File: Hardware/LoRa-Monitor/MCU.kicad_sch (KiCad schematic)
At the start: 20 parts, among them U1 ESP32-S3-WROOM-1

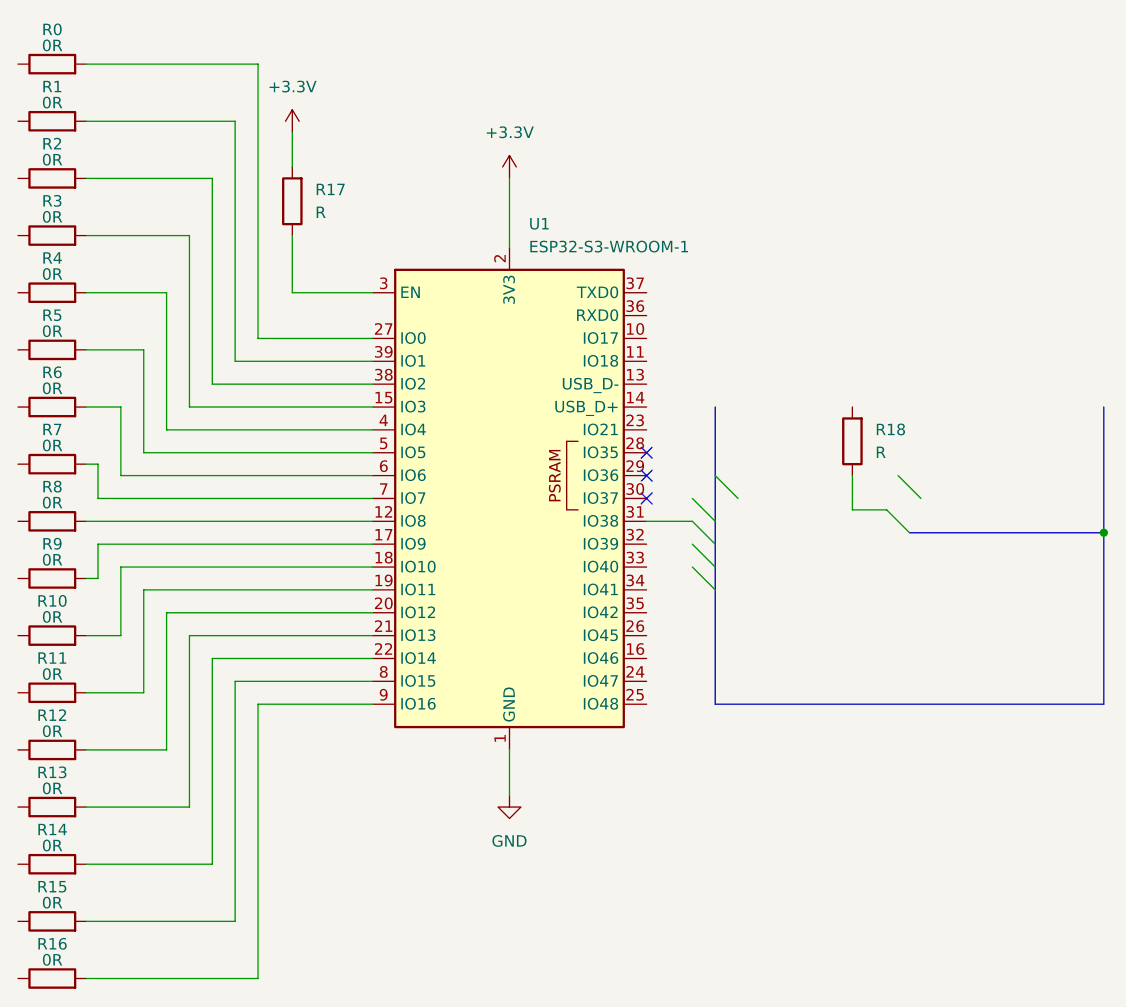
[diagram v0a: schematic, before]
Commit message: Added PSU
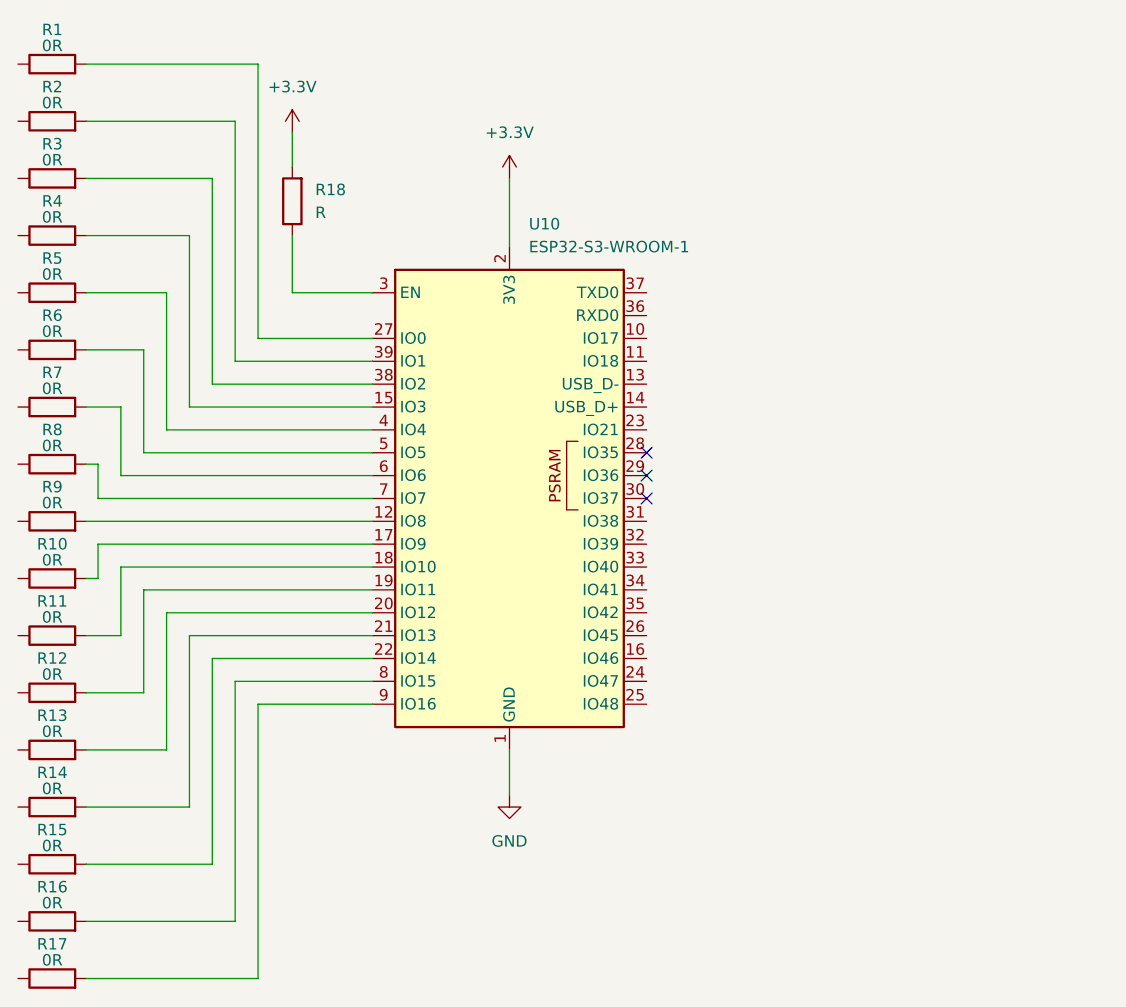
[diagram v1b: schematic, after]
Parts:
- removed R18: R, Resistor_SMD:R_0805_2012Metric, symbol Device:R
- removed U1: ESP32-S3-WROOM-1, Package_DFN_QFN:QFN-56-1EP_7x7mm_P0.4mm_EP4x4mm, symbol RF_Module:ESP32-S3-WROOM-1
- added U10: ESP32-S3-WROOM-1, RF_Module:ESP32-S3-WROOM-1, symbol RF_Module:ESP32-S3-WROOM-1
- renumbered R0 to R1, R9 to R10, R10 to R11, R11 to R12, R12 to R13, R13 to R14, R14 to R15, R15 to R16, R16 to R17, R17 to R18, R1 to R2, R2 to R3, R3 to R4, R4 to R5, R5 to R6, R6 to R7, R7 to R8, R8 to R9
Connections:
- net +3.3V: now also U10.2 (3V3)
- net GND: now also U10.1 (GND), U10.40 (GND), U10.41 (GND)
- net at R16.2: now also U10.8 (IO15)
- net at R2.2: now also U10.39 (IO1)
- net at R9.2: now also U10.12 (IO8)
- net at R6.2: now also U10.5 (IO5)
- net at R1.2: now also U10.27 (IO0)
- net at R15.2: now also U10.22 (IO14)
- net at R5.2: now also U10.4 (IO4)
- net at R4.2: now also U10.15 (IO3)
- net at R10.2: now also U10.17 (IO9)
- net at R11.2: now also U10.18 (IO10)
- net at R12.2: now also U10.19 (IO11)
- net at R13.2: now also U10.20 (IO12)
- net at R14.2: now also U10.21 (IO13)
- net at R18.1: now also U10.3 (EN)
- net at R3.2: now also U10.38 (IO2)
- net at R7.2: now also U10.6 (IO6)
- net at R8.2: now also U10.7 (IO7)
- net at R17.2: now also U10.9 (IO16)

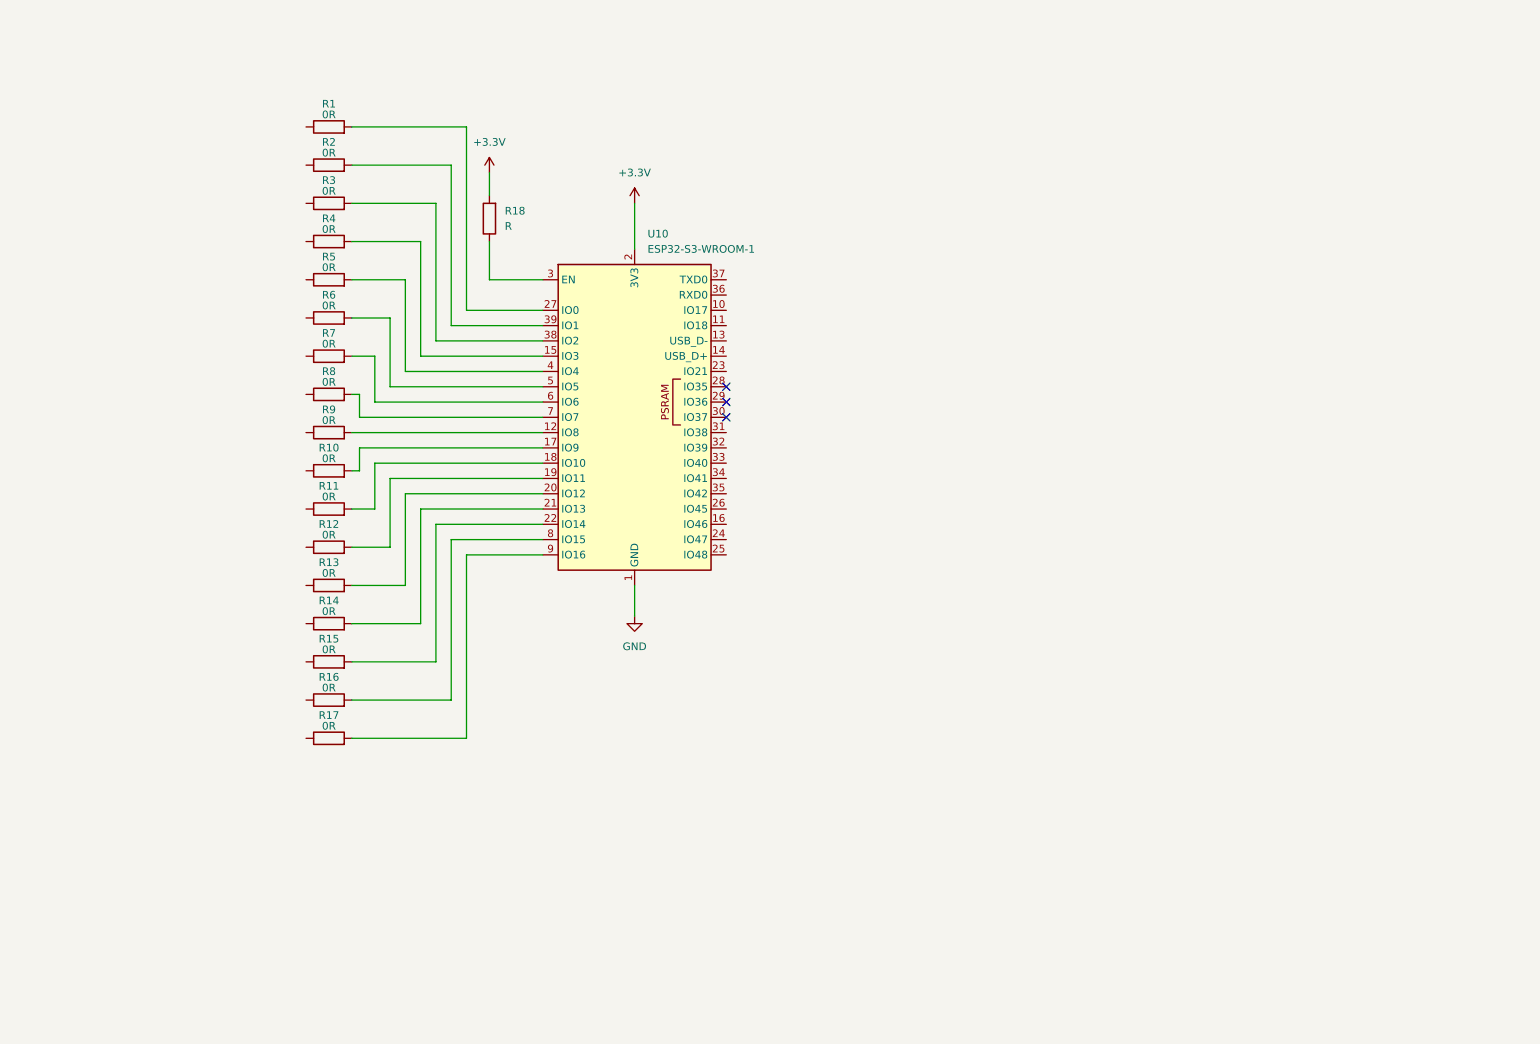
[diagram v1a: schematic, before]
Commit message: Finished Energy Meter Module, started LoRa Module and MCU.
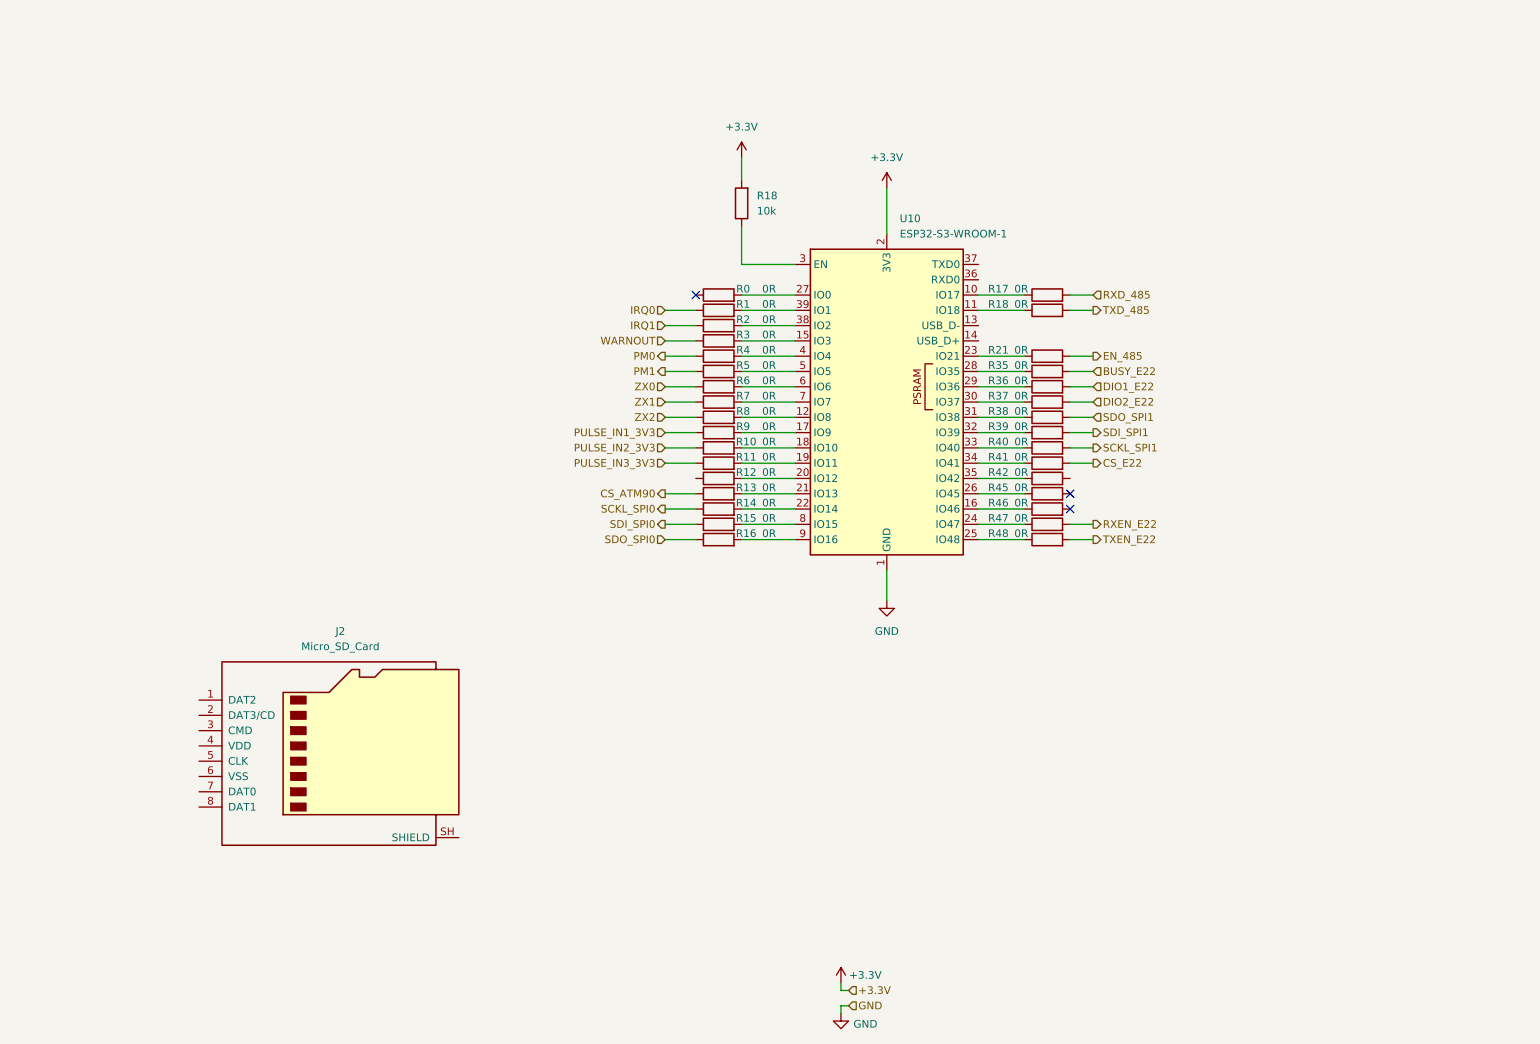
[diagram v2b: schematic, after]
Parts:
- added J2: Micro_SD_Card, Connector_Card:microSD_HC_Molex_47219-2001, symbol Connector:Micro_SD_Card
- added R0, R18, R21, R35, R36, R37, R38, R39, R40, R41, R42, R45, R46, R47, R48: 0R, Resistor_SMD:R_0805_2012Metric, symbol Device:R
- R18: value R -> 10k
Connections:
- net SDO_SPI0: now reaches R16.1
- net at U10.8 (IO15): now also R15.2; no longer R16.2
- net IRQ1: now reaches R2.1
- net at R2.2: now also U10.38 (IO2); no longer U10.39 (IO1)
- net PULSE_IN1_3V3: now reaches R9.1
- net at U10.12 (IO8): now also R8.2; no longer R9.2
- net at U10.10 (IO17): now also R17.1
- net at U10.11 (IO18): now also R18.1
- net at R4.2: now also U10.4 (IO4); no longer U10.15 (IO3)
- net at U10.16 (IO46): now also R46.1
- net at U10.17 (IO9): now also R9.2; no longer R10.2
- net at U10.18 (IO10): now also R10.2; no longer R11.2
- net at U10.19 (IO11): now also R11.2; no longer R12.2
- net at R13.2: now also U10.21 (IO13); no longer U10.20 (IO12)
- net at R14.2: now also U10.22 (IO14); no longer U10.21 (IO13)
- net at U10.23 (IO21): now also R21.1
- net at U10.24 (IO47): now also R47.1
- net at U10.25 (IO48): now also R48.1
- net at U10.26 (IO45): now also R45.1
- net at U10.27 (IO0): now also R0.2; no longer R1.2
- net at U10.28 (IO35): now also R35.1
- net at U10.29 (IO36): now also R36.1
- net at U10.30 (IO37): now also R37.1
- net at U10.31 (IO38): now also R38.1
- net at U10.32 (IO39): now also R39.1
- net at U10.33 (IO40): now also R40.1
- net at U10.34 (IO41): now also R41.1
- net at U10.35 (IO42): now also R42.1
- net at R3.2: now also U10.15 (IO3); no longer U10.38 (IO2)
- net at R5.2: now also U10.5 (IO5); no longer U10.4 (IO4)
- net at R6.2: now also U10.6 (IO6); no longer U10.5 (IO5)
- net at R7.2: now also U10.7 (IO7); no longer U10.6 (IO6)
- net at U10.9 (IO16): now also R16.2; no longer R17.2
- net ZX0: now reaches R6.1
- net IRQ0: now reaches R1.1
- net SDI_SPI0: now reaches R15.1
- net PM1: now reaches R5.1
- net PULSE_IN3_3V3: now reaches R11.1
- net PULSE_IN2_3V3: now reaches R10.1
- net CS_ATM90: now reaches R13.1
- net ZX1: now reaches R7.1
- net SCKL_SPI0: now reaches R14.1
- net WARNOUT: now reaches R3.1
- net PM0: now reaches R4.1
- net ZX2: now reaches R8.1
- new net: R12.2, U10.20 (IO12)
- new net: R1.2, U10.39 (IO1)
- new net BUSY_E22: R35.2
- new net CS_E22: R41.2
- new net DIO1_E22: R36.2
- new net DIO2_E22: R37.2
- new net EN_485: R21.2
- new net RXD_485: R17.2
- new net RXEN_E22: R47.2
- new net SCKL_SPI1: R40.2
- new net SDI_SPI1: R39.2
- new net SDO_SPI1: R38.2
- new net TXD_485: R18.2
- new net TXEN_E22: R48.2
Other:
- moved on the sheet: R18, U10

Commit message: Finished MCU and Lora modules. Finished Connectors sheet
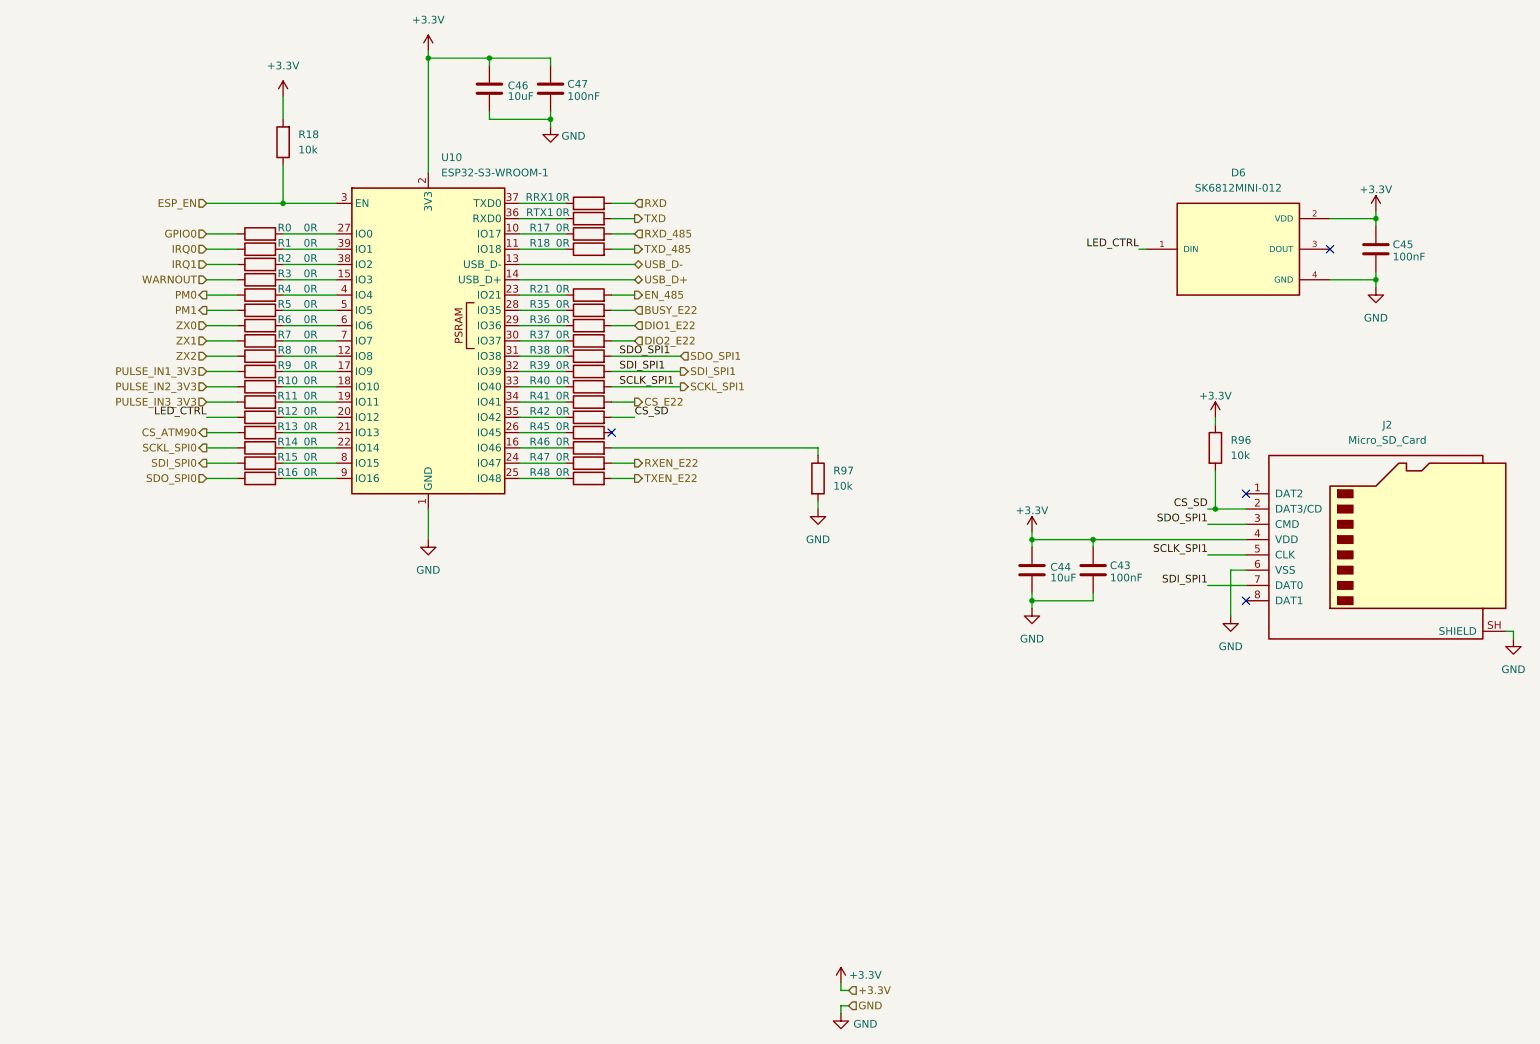
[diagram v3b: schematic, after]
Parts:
- added C43, C45, C47: 100nF, Capacitor_SMD:C_0805_2012Metric, symbol Device:C
- added C44, C46: 10uF, Capacitor_SMD:C_0805_2012Metric, symbol Device:C
- added D6: SK6812MINI-012, DeviceComponents:LED_SK6812MINI-012, symbol DeviceComponents:SK6812MINI-012
- added R96, R97: 10k, Resistor_SMD:R_0805_2012Metric, symbol Device:R
- added RRX1, RTX1: 0R, Resistor_SMD:R_0805_2012Metric, symbol Device:R
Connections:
- net +3.3V: now also J2.4 (VDD), C43.1, C44.1, C45.1, C46.1, C47.1, D6.2 (VDD), R96.1
- net GND: now also J2.6 (VSS), J2.SH (SHIELD), C43.2, C44.2, C45.2, C46.2, C47.2, D6.4 (GND), R97.2
- net SCKL_SPI1: now also J2.5 (CLK)
- net SDI_SPI1: now also J2.7 (DAT0)
- net SDO_SPI1: now also J2.3 (CMD)
- net GPIO0: now reaches R0.1
- net USB_D-: now reaches U10.13 (USB_D-)
- net USB_D+: now reaches U10.14 (USB_D+)
- net ESP_EN: now reaches R18.1, U10.3 (EN)
- net at U10.36 (RXD0): now also RTX1.1
- net at U10.37 (TXD0): now also RRX1.1
- net CS_SD: now reaches R42.2
- net CS_SD: now also J2.2 (DAT3/CD), R96.2
- net LED_CTRL: now reaches R12.1
- net LED_CTRL: now also D6.1 (DIN)
- net at R46.2: now also R97.1
- new net RXD: RRX1.2
- new net TXD: RTX1.2
- no-connect marks 3 -> 4
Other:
- moved on the sheet: J2, R0, R1, R10, R11, R12, R13, R14, R15, R16, R17, R18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
